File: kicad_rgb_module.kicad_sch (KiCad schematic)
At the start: 29 parts, among them J1 Conn_HackConnect, SW1 TS-1088-AR02016, U1 STM32G030F6P6, U2 NCP114ASN330T1G, Y1 Crystal_GND_4_Pin

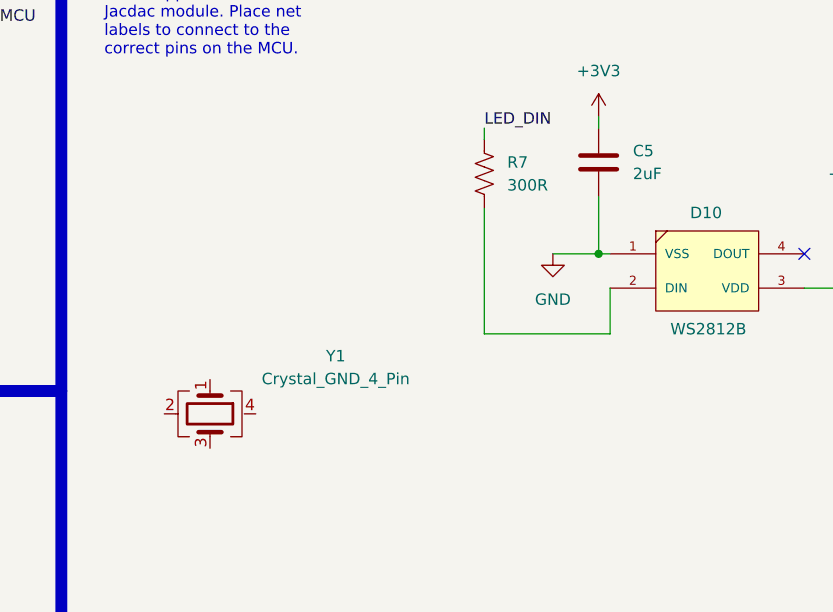
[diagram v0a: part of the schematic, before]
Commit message: reverting unncessary change to .kicad_* files & sym-lib-table
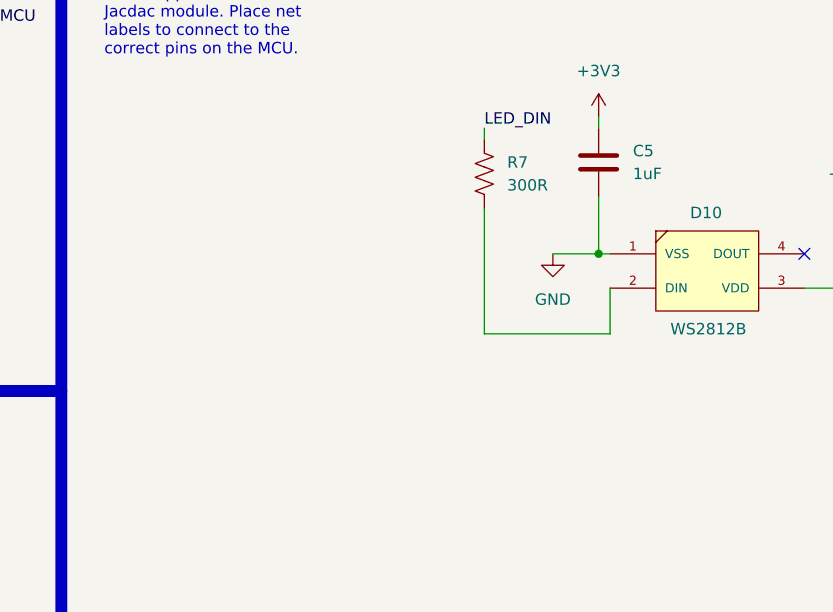
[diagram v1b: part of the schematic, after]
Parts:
- removed Y1: Crystal_GND_4_Pin, Crystal:Crystal_SMD_3225-4Pin_3.2x2.5mm, symbol Crystal:Crystal_GND_4_Pin
- C5: value 2uF -> 1uF
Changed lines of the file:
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@@
-	)
-	(symbol
-		(lib_id "Crystal:Crystal_GND_4_Pin")
-		(at 160.02 140.97 270)
-		(unit 1)
-		(exclude_from_sim no)
-		(in_bom yes)
-		(on_board yes)
-		(dnp no)
-		(fields_autoplaced yes)
-		(property "Reference" "Y1"
-			(at 173.99 134.5498 90)
-			(effects
-				(font
-					(size 1.27 1.27)
-				)
-			)
-		)
-		(property "Value" "Crystal_GND_4_Pin"
-			(at 173.99 137.0898 90)
-			(effects
-				(font
-					(size 1.27 1.27)
-				)
-			)
-		)
-		(property "Footprint" "Crystal:Crystal_SMD_3225-4Pin_3.2x2.5mm"
-			(at 160.02 140.97 0)
-			(effects
-				(font
-					(size 1.27 1.27)
-				)
-				(hide yes)
-			)
-		)
-		(property "Datasheet" "~"
-			(at 160.02 140.97 0)
-			(effects
-				(font
-					(size 1.27 1.27)
-				)
-				(hide yes)
-			)
-		)
-		(property "Description" "Four pin crystal, GND on pins 2 and 4"
-			(at 160.02 140.97 0)
-			(effects
-				(font
-					(size 1.27 1.27)
-				)
-				(hide yes)
-			)
-		)
-		(property private "KLC_S3.3" "The rectangle is not a symbol body but a graphical element"
-			(at 147.32 140.97 0)
-			(show_name yes)
-			(effects
-				(font
-					(size 1.27 1.27)
-				)
-				(hide yes)
-			)
-		)
-		(property private "KLC_S4.1" "Some pins are on 50mil grid to make the symbol small"
-			(at 144.78 140.97 0)
-			(show_name yes)
-			(effects
-				(font
-					(size 1.27 1.27)
-				)
-				(hide yes)
-			)
-		)
-		(property "LCSC" "C5203640"
-			(at 160.02 140.97 90)
-			(effects
-				(font
-					(size 1.27 1.27)
-				)
-				(hide yes)
-			)
-		)
-		(pin "4"
-		)
-		(pin "3"
-		)
-		(pin "4"
-		)
-		(pin "4"
-		)
-		(pin "2"
-		)
-		(pin "1"
-		)
-		(instances
-			(project ""
-				(path "/9a8e7fbc-34f9-4889-88fa-a265258a8f63"
-					(reference "Y1")
-					(unit 1)
-				)
-			)
-		)
 	)
 	(symbol
@@
 			)
 		)
-		(property "Value" "2uF"
+		(property "Value" "1uF"
 			(at 207.01 114.2999 0)
 			(effects

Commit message: meta/ dir required for template in Kicad
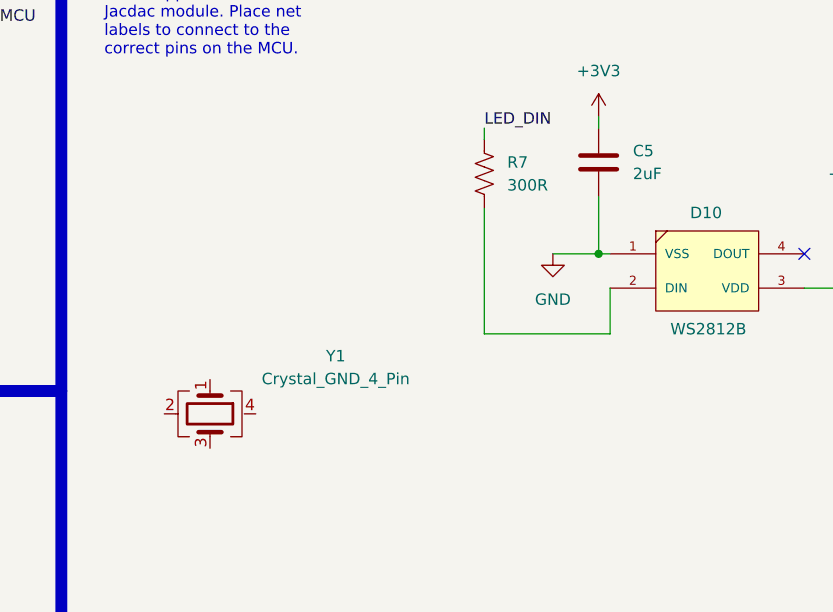
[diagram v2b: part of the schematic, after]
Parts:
- added Y1: Crystal_GND_4_Pin, Crystal:Crystal_SMD_3225-4Pin_3.2x2.5mm, symbol Crystal:Crystal_GND_4_Pin
- C5: value 1uF -> 2uF
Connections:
- new net: Y1.2, Y1.4 (G)
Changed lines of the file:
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@@
+	)
+	(symbol
+		(lib_id "Crystal:Crystal_GND_4_Pin")
+		(at 160.02 140.97 270)
+		(unit 1)
+		(exclude_from_sim no)
+		(in_bom yes)
+		(on_board yes)
+		(dnp no)
+		(fields_autoplaced yes)
+		(property "Reference" "Y1"
+			(at 173.99 134.5498 90)
+			(effects
+				(font
+					(size 1.27 1.27)
+				)
+			)
+		)
+		(property "Value" "Crystal_GND_4_Pin"
+			(at 173.99 137.0898 90)
+			(effects
+				(font
+					(size 1.27 1.27)
+				)
+			)
+		)
+		(property "Footprint" "Crystal:Crystal_SMD_3225-4Pin_3.2x2.5mm"
+			(at 160.02 140.97 0)
+			(effects
+				(font
+					(size 1.27 1.27)
+				)
+				(hide yes)
+			)
+		)
+		(property "Datasheet" "~"
+			(at 160.02 140.97 0)
+			(effects
+				(font
+					(size 1.27 1.27)
+				)
+				(hide yes)
+			)
+		)
+		(property "Description" "Four pin crystal, GND on pins 2 and 4"
+			(at 160.02 140.97 0)
+			(effects
+				(font
+					(size 1.27 1.27)
+				)
+				(hide yes)
+			)
+		)
+		(property private "KLC_S3.3" "The rectangle is not a symbol body but a graphical element"
+			(at 147.32 140.97 0)
+			(show_name yes)
+			(effects
+				(font
+					(size 1.27 1.27)
+				)
+				(hide yes)
+			)
+		)
+		(property private "KLC_S4.1" "Some pins are on 50mil grid to make the symbol small"
+			(at 144.78 140.97 0)
+			(show_name yes)
+			(effects
+				(font
+					(size 1.27 1.27)
+				)
+				(hide yes)
+			)
+		)
+		(property "LCSC" "C5203640"
+			(at 160.02 140.97 90)
+			(effects
+				(font
+					(size 1.27 1.27)
+				)
+				(hide yes)
+			)
+		)
+		(pin "4"
+		)
+		(pin "3"
+		)
+		(pin "4"
+		)
+		(pin "4"
+		)
+		(pin "2"
+		)
+		(pin "1"
+		)
+		(instances
+			(project ""
+				(path "/9a8e7fbc-34f9-4889-88fa-a265258a8f63"
+					(reference "Y1")
+					(unit 1)
+				)
+			)
+		)
 	)
 	(symbol
@@
 			)
 		)
-		(property "Value" "1uF"
+		(property "Value" "2uF"
 			(at 207.01 114.2999 0)
 			(effects
